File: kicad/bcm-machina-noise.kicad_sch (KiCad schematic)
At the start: 61 parts, among them J1 USB_A, J2 AVR-ISP-6, J3 AudioJack2_SwitchT, J5 AudioJack2_SwitchT, Q1 2N5457, Q2 2N5457, SW1 SW_Push, SW2 SW_Push, U1 4069, U2 MCP602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

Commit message: Updating schematic with fixes and changes
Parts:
- removed RV3: 10k, Trimpot:Potentiometer_THT_Bourns_3306P_Vertical, symbol Device:R_Potentiometer_Trim
- added R24: 220k, Resistor_THT:R_Axial_DIN0207_L6.3mm_D2.5mm_P10.16mm_Horizontal, symbol Device:R
- added R25, R27: 1k, Resistor_THT:R_Axial_DIN0207_L6.3mm_D2.5mm_P10.16mm_Horizontal, symbol Device:R
- added R26: 47k, Resistor_THT:R_Axial_DIN0207_L6.3mm_D2.5mm_P10.16mm_Horizontal, symbol Device:R
- C1, C2: value 100nF -> 220nF
- C4, C5: value C_Polarized -> 10uF
- C8: value 10nF -> 100nF
- Q1, Q2: value 2N5457 -> J113
- R13, R14, R17: value 10k -> 100k
- R16: value 10k -> 1k
- RV1: value 10kA -> 100k
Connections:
- net GND: no longer R16.1
- net MCU_DOUT1: now also U3.6 (PA7); no longer J2.4 (MOSI), U3.7 (PA6)
- net at C1.2, U1.4: now also R25.1, R27.1; no longer Q2.3 (S), RV1.5
- net at R14.1, R17.2, U1.1: now also R13.2, R24.1; no longer U1.12
- net at R14.2, U1.2: now also R16.1; no longer Q1.3 (S), RV1.2
- net at C2.2, C5.1, U1.6: now also R17.1; no longer R16.2, RV2.3
- net at C4.2: now also R24.2; no longer R13.1
- net at U1.13: now also RV2.1, RV2.2, R26.1; no longer R13.2
- net at RV1.4: now also Q2.3 (S), RV1.5, R25.2
- net at RV1.1: now also Q1.3 (S), R16.2, RV1.2
- net MCU_PWM_2 renamed MCU_MOSI
- net MCU_MOSI: now also J2.4 (MOSI), U3.7 (PA6); no longer U3.6 (PA7)
- new net: R27.2, RV2.3
- new net: R13.1, R26.2, U1.12
- no-connect marks 13 -> 9
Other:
- note added: "Adjusts overall gain of filter Higher values mean lower gain"
- note added: "Gain varies from 47/101 to 47/1 or 0.46 to 47. This directly corelates to the resonance"
- note added: "Might not be necessary"
- note added: "cutoff = 1/(2 * pi * R * C) = 1/(2 * 3.14 * 10000 * (100*10^9)) = 159Hz Using a low cutoff given this signal should be LFO rate"
- note added: "is this needed?"
- moved on the sheet: C1, C2, C3, C4, C5, C7, C8, J3, J5, Q1, Q2, R13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

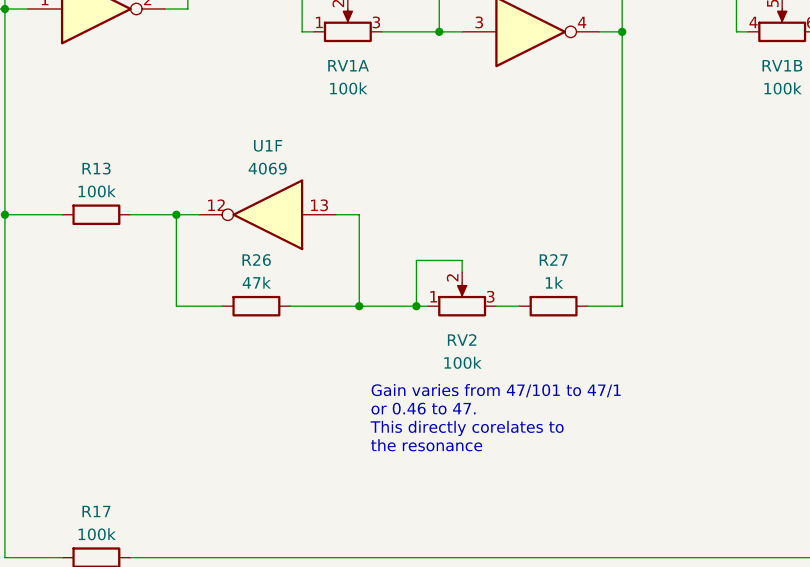
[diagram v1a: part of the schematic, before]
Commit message: more tweaks to resonance values
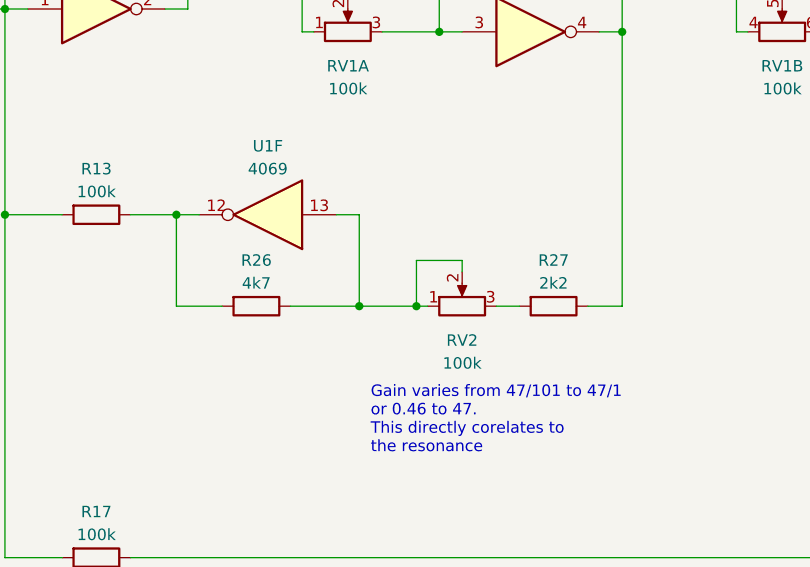
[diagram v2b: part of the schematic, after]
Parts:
- R26: value 47k -> 4k7
- R27: value 1k -> 2k2
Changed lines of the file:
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@@
       (effects (font (size 1.27 1.27)))
     )
-    (property "Value" "1k" (at 273.05 120.65 90)
+    (property "Value" "2k2" (at 273.05 120.65 90)
       (effects (font (size 1.27 1.27)))
     )
@@
       (effects (font (size 1.27 1.27)))
     )
-    (property "Value" "47k" (at 240.03 120.65 90)
-      (effects (font (size 1.27 1.27)))
-    )
+    (property "Value" "4k7" (at 240.03 120.65 90)
+      (effects (font (size 1.27 1.27)))
+    )

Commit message: A few more schematic tweaks
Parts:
- added C9: 100pF, Capacitor_THT:C_Rect_L7.0mm_W3.5mm_P5.00mm, symbol Device:C
- added R28, R29, R30: 100k, Resistor_THT:R_Axial_DIN0207_L6.3mm_D2.5mm_P10.16mm_Horizontal, symbol Device:R
- added TP1: OSC Test Point, TestPoint:TestPoint_Loop_D2.50mm_Drill1.0mm_LowProfile, symbol Connector:TestPoint
- added TP2: LFO Test Point, TestPoint:TestPoint_Loop_D2.50mm_Drill1.0mm_LowProfile, symbol Connector:TestPoint
- R24: value 220k -> 100k
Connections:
- net GND: now also C9.1
- net MCU_MISO: now also R28.2; no longer C4.1
- net at C1.1, Q1.1 (D), RV1.3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: now also R30.1
- net at C2.1, Q2.1 (D), RV1.6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: now also R29.1
- net at Q1.3 (S), R16.2, RV1.1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: now also R30.2
- net at Q2.3 (S), R25.2, RV1.4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: now also R29.2
- net at R23.1, U2.1, U2.2 (-): now also TP2.1
- new net: C4.1, C9.2, R28.1, TP1.1
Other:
- note added: "R29 and R30 are just here to help with testing they won't be in the final build"
- note added: "cutoff = 1/(2 * pi * R * C) = 1/(2 * 3.14 * 10000 * (100*10^12)) = 15915Hz This is some initial filtering to start removing the PWM signal R28 should also sum with R24 to set the gain of the filter to 0.5 Worth testing if this is useful"
- note removed: "Adjusts overall gain of filter Higher values mean lower gain"
- moved on the sheet: C4, R24

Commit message: Updating usb power connection
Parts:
- removed J1: USB_A, USBPower:AMPHENOL_10103593-0001LF, symbol Connector:USB_A
- added J4: USB_B_Micro, USBPower:AMPHENOL_10103593-0001LF, symbol Connector:USB_B_Micro
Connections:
- net GND: now also J4.5 (GND), J4.6 (Shield)
- net VCC: now also J4.1 (VBUS)
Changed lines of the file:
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@@
   (junction (at 328.93 85.09) (diameter 0) (color 0 0 0 0)
   )
+  (junction (at 38.1 58.42) (diameter 0) (color 0 0 0 0)
+  )
   (junction (at 245.11 78.74) (diameter 0) (color 0 0 0 0)
   )
@@
   )
   (no_connect (at 335.28 52.07))
-  (no_connect (at 38.1 57.15))
   (no_connect (at 45.72 49.53))
   (no_connect (at 165.1 173.99))
@@
   (no_connect (at 92.71 119.38))
   (no_connect (at 92.71 116.84))
+  (no_connect (at 45.72 52.07))
   (wire (pts (xy 280.67 78.74) (xy 280.67 92.71))
     (stroke (width 0) (type default))
@@
     (stroke (width 0) (type default))
   )
+  (wire (pts (xy 38.1 57.15) (xy 38.1 58.42))
+    (stroke (width 0) (type default))
+  )
   (wire (pts (xy 87.63 121.92) (xy 92.71 121.92))
     (stroke (width 0) (type default))
@@
     (stroke (width 0) (type default))
   )
+  (wire (pts (xy 38.1 58.42) (xy 41.91 58.42))
+    (stroke (width 0) (type default))
+  )
   (wire (pts (xy 144.78 90.17) (xy 157.48 90.17))
     (stroke (width 0) (type default))
@@
     (stroke (width 0) (type default))
   )
-  (wire (pts (xy 35.56 58.42) (xy 41.91 58.42))
+  (wire (pts (xy 35.56 58.42) (xy 38.1 58.42))
     (stroke (width 0) (type default))
   )
@@
     )
   )
-  (symbol (lib_id "Connector:USB_A") (at 38.1 46.99 0) (unit 1)
-    (in_bom yes) (on_board yes) (dnp no) (fields_autoplaced)
-    (property "Reference" "J1" (at 38.1 35.56 0)
-      (effects (font (size 1.27 1.27)))
-    )
-    (property "Value" "USB_A" (at 38.1 38.1 0)
-      (effects (font (size 1.27 1.27)))
-    )
-    (property "Footprint" "USBPower:AMPHENOL_10103593-0001LF" (at 41.91 48.26 0)
-      (effects (font (size 1.27 1.27)) hide)
-    )
-    (property "Datasheet" " ~" (at 41.91 48.26 0)
-      (effects (font (size 1.27 1.27)) hide)
-    )
-    (pin "1")
-    (pin "2")
-    (pin "3")
-    (pin "4")
-    (pin "5")
-    (instances
-      (project "bcm-machina-noise"
-        (path "/5b0acaca-dc50-4fa5-b146-164c1b9ad031"
-          (reference "J1") (unit 1)
-        )
-      )
-    )
-  )
   (symbol (lib_id "Device:R_Potentiometer_Dual_Separate") (at 250.19 92.71 90) (unit 1)
     (in_bom yes) (on_board yes) (dnp no)
@@
         )
       )
+    )
+  )
+  (symbol (lib_id "Connector:USB_B_Micro") (at 38.1 46.99 0) (unit 1)
+    (in_bom yes) (on_board yes) (dnp no) (fields_autoplaced)
+    (property "Reference" "J4" (at 38.1 35.56 0)
+      (effects (font (size 1.27 1.27)))
+    )
+    (property "Value" "USB_B_Micro" (at 38.1 38.1 0)
+      (effects (font (size 1.27 1.27)))
+    )
+    (property "Footprint" "USBPower:AMPHENOL_10103593-0001LF" (at 41.91 48.26 0)
+      (effects (font (size 1.27 1.27)) hide)
+    )
+    (property "Datasheet" "~" (at 41.91 48.26 0)
+      (effects (font (size 1.27 1.27)) hide)
+    )
+    (pin "1")
+    (pin "2")
+    (pin "3")
+    (pin "4")
+    (pin "5")
+    (pin "6")
+    (instances
+      (project "bcm-machina-noise"
+        (path "/5b0acaca-dc50-4fa5-b146-164c1b9ad031"
+          (reference "J4") (unit 1)
+        )
+      )

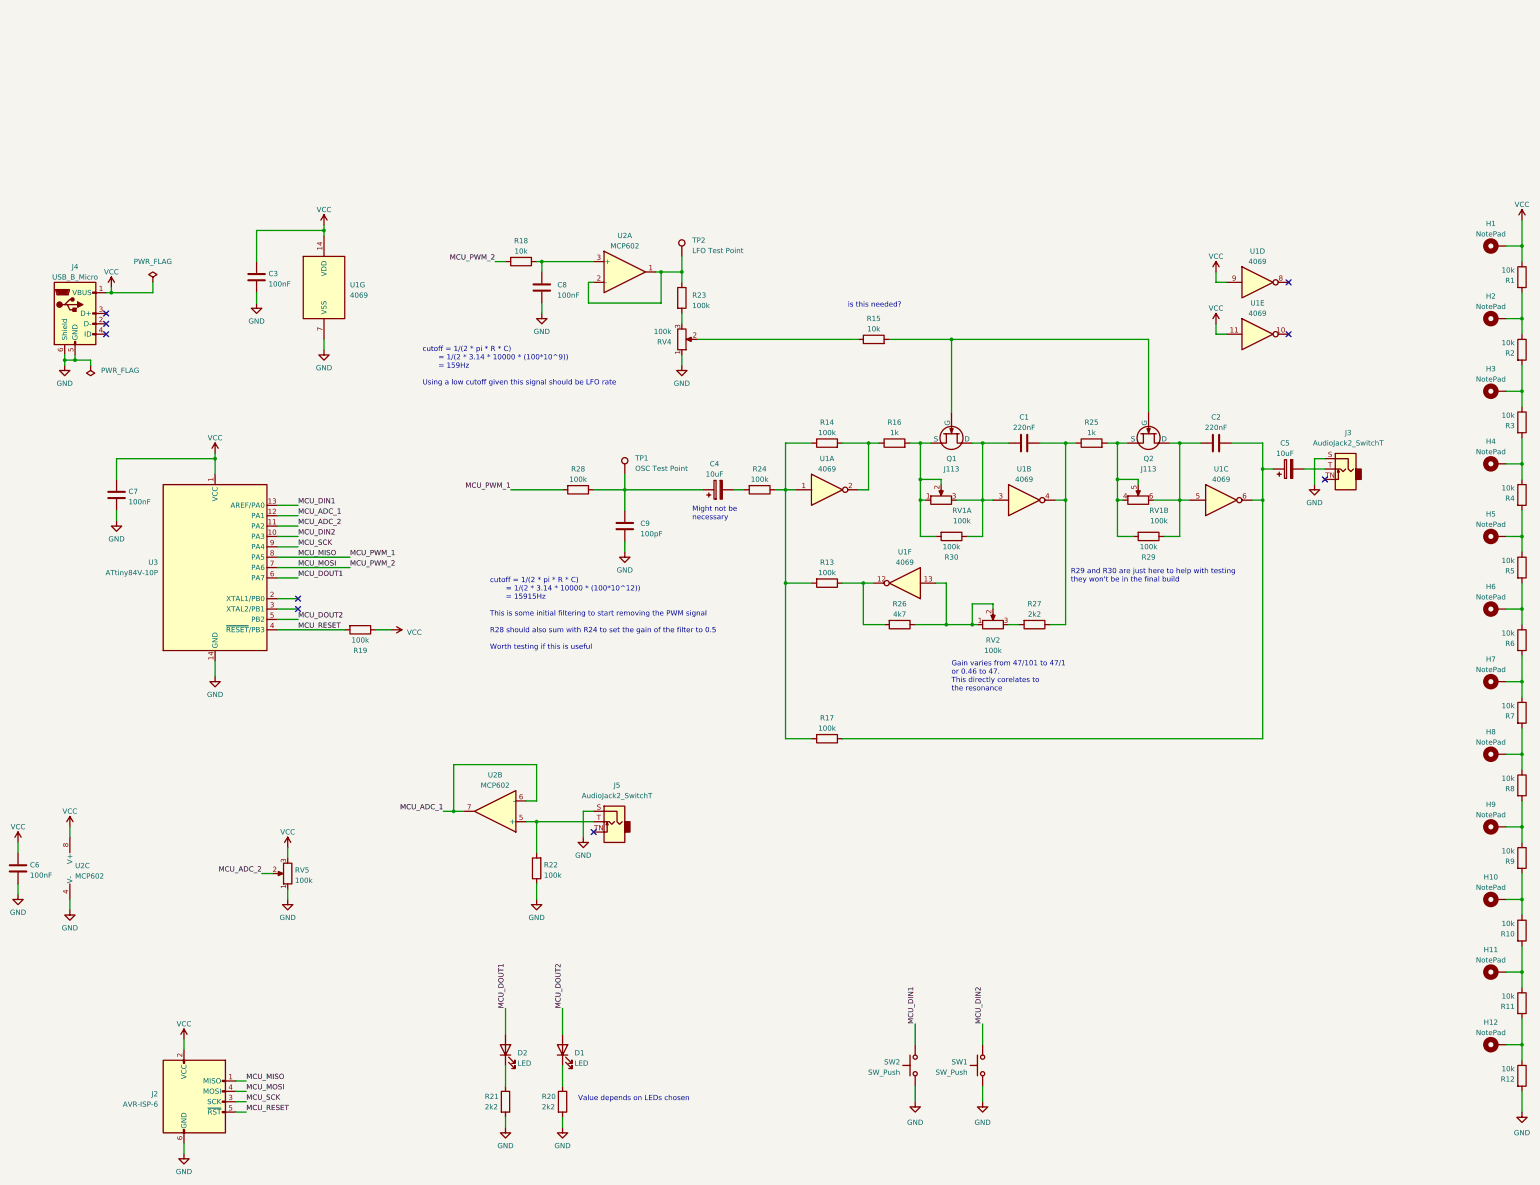
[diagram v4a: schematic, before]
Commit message: Tweaks to circuitry
Fixing bugs
Changing some values
Adding another potentiometer
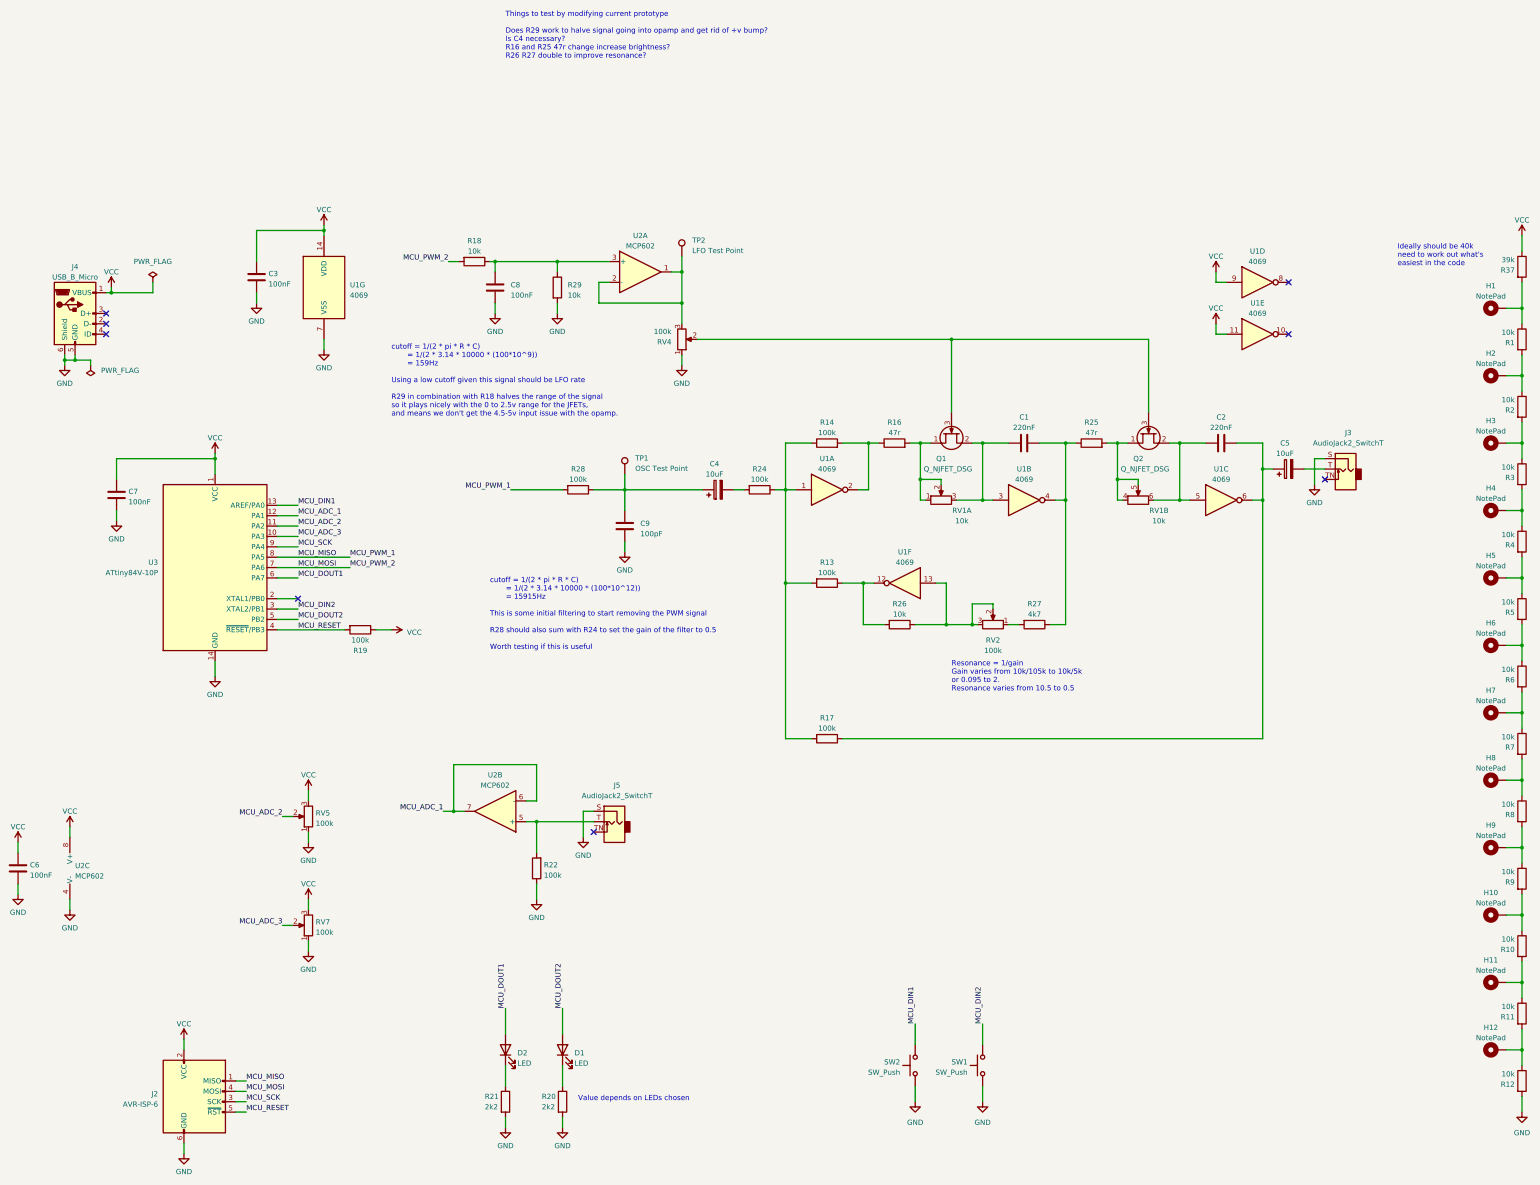
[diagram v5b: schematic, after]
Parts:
- removed Q1, Q2: J113, Package_TO_SOT_THT:TO-92L_Inline_Wide, symbol Simulation_SPICE:NJFET
- removed R15: 10k, Resistor_THT:R_Axial_DIN0207_L6.3mm_D2.5mm_P10.16mm_Horizontal, symbol Device:R
- removed R23, R30: 100k, Resistor_THT:R_Axial_DIN0207_L6.3mm_D2.5mm_P10.16mm_Horizontal, symbol Device:R
- added Q1, Q2: Q_NJFET_DSG, Rumblesan_Standard_Parts:TO-92_Inline_Wide, symbol Device:Q_NJFET_DSG
- added R37: 39k, Resistor_THT:R_Axial_DIN0207_L6.3mm_D2.5mm_P10.16mm_Horizontal, symbol Device:R
- added RV7: 100k, Potentiometer_THT:Potentiometer_Alpha_RD901F-40-00D_Single_Vertical_CircularHoles, symbol Device:R_Potentiometer
- R16, R25: value 1k -> 47r
- R26: value 4k7 -> 10k
- R27: value 2k2 -> 4k7
- R29, RV1: value 100k -> 10k
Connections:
- net GND: now also R29.2, RV7.1
- net MCU_DIN2: now also U3.3 (XTAL2/PB1); no longer U3.10 (PA3)
- net VCC: now also R37.1, RV7.3; no longer H1.1, R1.1
- net at R27.2: now also RV2.1; no longer RV2.3
- net at C1.1, RV1.3, U1.3: now also Q1.2 (S)
- net at C2.1, RV1.6, U1.5: now also Q2.2 (S); no longer R29.1
- net at R16.2, RV1.1, RV1.2: now also Q1.1 (D)
- net at R25.2, RV1.4, RV1.5: now also Q2.1 (D); no longer R29.2
- net at TP2.1, U2.1, U2.2 (-): now also RV4.3
- net at RV4.2: now also Q1.3 (G), Q2.3 (G)
- net at C8.2, R18.1, U2.3 (+): now also R29.1
- net at R26.1, RV2.2, U1.13: now also RV2.3; no longer RV2.1
- new net: H1.1, R1.1, R37.2
- new net MCU_ADC_3: RV7.2, U3.10 (PA3)
- no-connect marks 9 -> 8
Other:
- note added: "Ideally should be 40k need to work out what's easiest in the code"
- note added: "Resonance = 1/gain Gain varies from 10k/105k to 10k/5k or 0.095 to 2. Resonance varies from 10.5 to 0.5"
- note added: "Things to test by modifying current prototype Does R29 work to halve signal going into opamp and get rid of +v bump? Is C4 necessary? R16 and R25 47r change increase brightness? R26 R27 double to improve resonance?"
- note added: "cutoff = 1/(2 * pi * R * C) = 1/(2 * 3.14 * 10000 * (100*10^9)) = 159Hz Using a low cutoff given this signal should be LFO rate R29 in combination with R18 halves the range of the signal so it plays nicely with the 0 to 2.5v range for the JFETs, and means we don't get the 4.5-5v input issue with the opamp."
- note removed: "Gain varies from 47/101 to 47/1 or 0.46 to 47. This directly corelates to the resonance"
- note removed: "Might not be necessary"
- note removed: "R29 and R30 are just here to help with testing they won't be in the final build"
- note removed: "cutoff = 1/(2 * pi * R * C) = 1/(2 * 3.14 * 10000 * (100*10^9)) = 159Hz Using a low cutoff given this signal should be LFO rate"
- note removed: "is this needed?"
- moved on the sheet: C2, C8, H1, H10, H11, H12, H2, H3, H4, H5, H6, H7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

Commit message: Changing pinout for the micro controller
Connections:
- net MCU_SCK is gone; now on net MCU_DIN2: J2.3 (SCK), U3.9 (PA4)
- net MCU_ADC_1: now also U3.13 (AREF/PA0); no longer U3.12 (PA1)
- net MCU_ADC_2: now also U3.12 (PA1); no longer U3.11 (PA2)
- net MCU_ADC_3: now also U3.11 (PA2); no longer U3.10 (PA3)
- net MCU_DIN1: now also U3.10 (PA3); no longer U3.13 (AREF/PA0)
- net MCU_DIN2: no longer U3.3 (XTAL2/PB1)
- no-connect marks 8 -> 9
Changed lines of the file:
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@@
   (junction (at 392.43 210.82) (diameter 0) (color 0 0 0 0)
   )
+  (no_connect (at 92.71 119.38))
   (no_connect (at 335.28 52.07))
   (no_connect (at 45.72 49.53))
@@
     (stroke (width 0) (type default))
   )
-  (wire (pts (xy 87.63 104.14) (xy 92.71 104.14))
+  (wire (pts (xy 87.63 104.14) (xy 105.41 104.14))
     (stroke (width 0) (type default))
   )
@@
     (effects (font (size 1.27 1.27)) (justify left bottom))
   )
-  (label "MCU_DIN1" (at 92.71 93.98 0) (fields_autoplaced)
+  (label "MCU_DIN1" (at 92.71 101.6 0) (fields_autoplaced)
     (effects (font (size 1.27 1.27)) (justify left bottom))
   )
@@
     (effects (font (size 1.27 1.27)) (justify left bottom))
   )
-  (label "MCU_ADC_2" (at 92.71 99.06 0) (fields_autoplaced)
+  (label "MCU_ADC_2" (at 92.71 96.52 0) (fields_autoplaced)
     (effects (font (size 1.27 1.27)) (justify left bottom))
   )
@@
     (effects (font (size 1.27 1.27)) (justify left bottom))
   )
-  (label "MCU_DIN2" (at 92.71 119.38 0) (fields_autoplaced)
+  (label "MCU_DIN2" (at 105.41 104.14 0) (fields_autoplaced)
     (effects (font (size 1.27 1.27)) (justify left bottom))
   )
@@
     (effects (font (size 1.27 1.27)) (justify left bottom))
   )
-  (label "MCU_ADC_3" (at 92.71 101.6 0) (fields_autoplaced)
+  (label "MCU_ADC_3" (at 92.71 99.06 0) (fields_autoplaced)
     (effects (font (size 1.27 1.27)) (justify left bottom))
   )
@@
     (effects (font (size 1.27 1.27)) (justify left bottom))
   )
-  (label "MCU_ADC_1" (at 92.71 96.52 0) (fields_autoplaced)
-    (effects (font (size 1.27 1.27)) (justify left bottom))
-  )
+  (label "MCU_ADC_1" (at 92.71 93.98 0) (fields_autoplaced)
+    (effects (font (size 1.27 1.27)) (justify left bottom))
+  )
